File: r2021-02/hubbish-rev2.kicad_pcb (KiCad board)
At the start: 4 copper layers, 100 x 100 mm, 118 parts, among them J1 Conn_01x06, J2 USB_A_Stacked, J3 USB_A_Stacked, J4 USB_A (female down), J5 Conn_01x03_Male, J6 USB_A_Stacked, J8 USB_A male UP, J9 USB_B_Micro (up), Q1 Si4435, U1 2k i2c eeprom, U10 NUP4202, U11 NUP4202, U12 NUP4202, U13 NUP4202, U14 NUP4202, U15 NUP4202, U16 NUP4202, U17 NUP4202, U18 SY8366H, U19 APL3511C, U2 SE5120ST33, U3 USB2517, U4 APL3511C, U5 APL3511C, U6 APL3511C, U7 APL3511C, U8 APL3511C, U9 APL3511C, Y1 24MHz

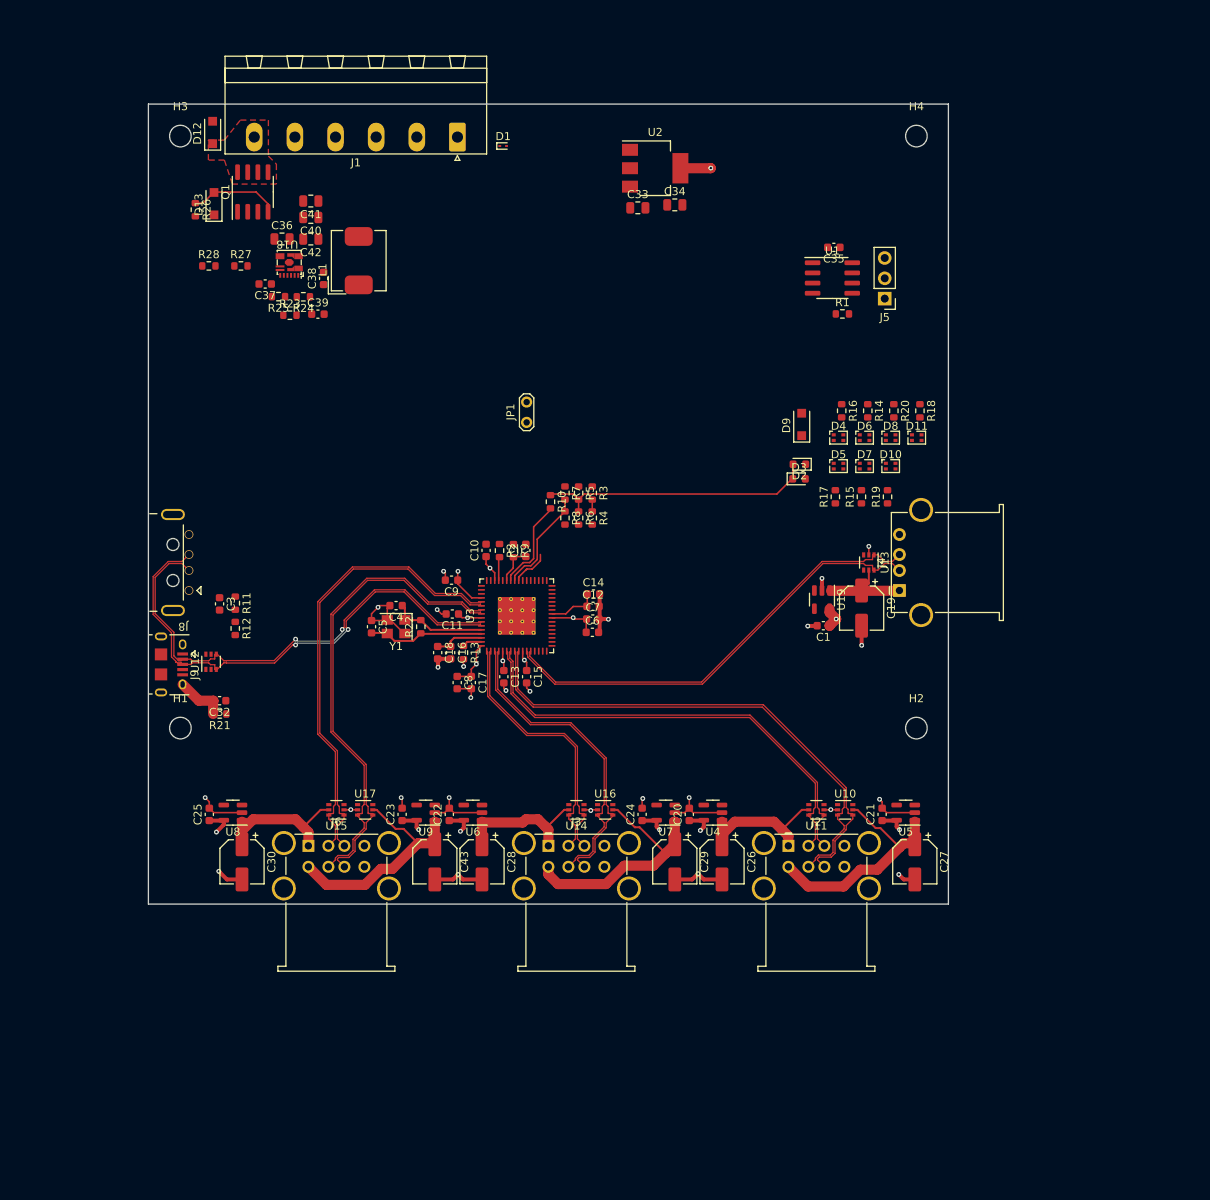
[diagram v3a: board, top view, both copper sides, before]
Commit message: r2021-02: "finish" routing
it's kinda untidy, but it's all routed out now, except for where I need
to replace the power supply
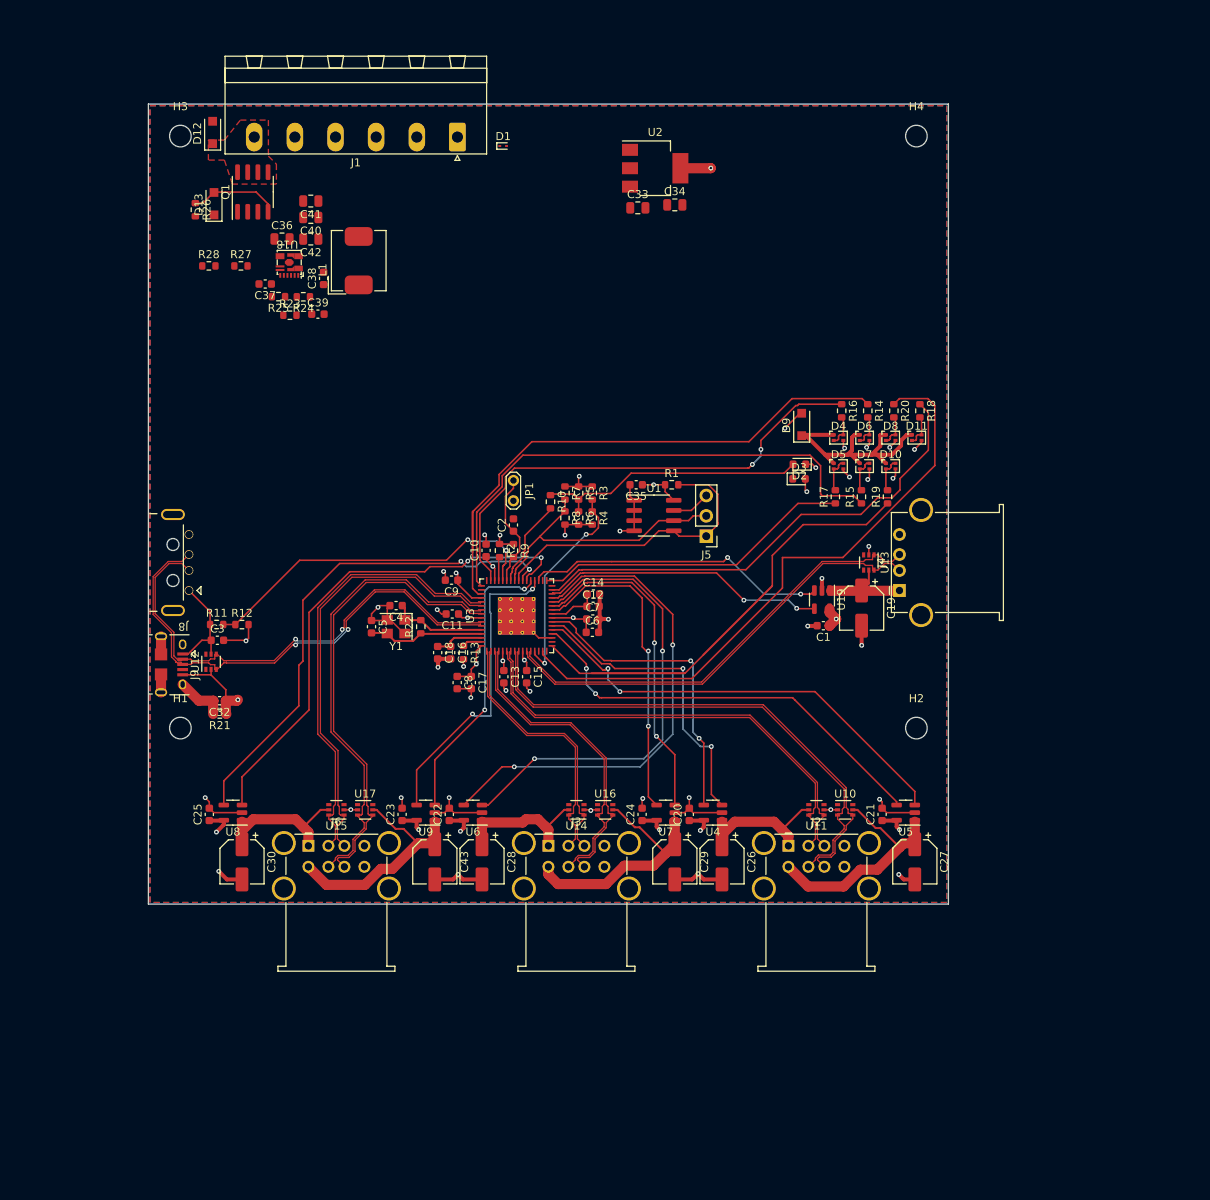
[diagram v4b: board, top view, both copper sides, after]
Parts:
- moved C35 38.6 mm to (141.0, 97.6)
- moved J5 37.1 mm to (149.7, 104.0)
- moved U1 37.1 mm to (143.2, 101.4)
- moved R1 30.2 mm to (145.4, 97.6)
- moved JP1 7.44 mm to (125.6, 97.0), turned to -90 degrees
- moved C3 4.55 mm to (88.6, 117.0), turned to 0 degrees
- moved R11 3.54 mm to (88.5, 115.1), turned to 0 degrees
- moved C2 3.53 mm to (125.6, 102.6)
- moved R12 0.97 mm to (91.7, 115.1), turned to 0 degrees
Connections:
- J5 pad 2: /upstream-config-leds/EE_SCL -> /upstream-config-leds/CFG_SEL0-EE_SCL
- U1 pad 6: /upstream-config-leds/EE_SCL -> /upstream-config-leds/CFG_SEL0-EE_SCL
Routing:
- net /upstream-config-leds/LED_A6: track 0.00 -> 78.3 mm
- net /upstream-config-leds/LED_A7: track 0.00 -> 77.2 mm
- net /upstream-config-leds/LED_A1: track 0.00 -> 72.6 mm
- net /upstream-config-leds/LED_A2: track 0.00 -> 65.9 mm
- net /downstream-port-power/OC5: track 0.00 -> 63.2 mm, vias 0 -> 2
- net /downstream-port-power/EN3: track 0.00 -> 63.0 mm, vias 0 -> 2
- net /downstream-port-power/EN5: track 0.00 -> 62.7 mm, vias 0 -> 2
- net /upstream-config-leds/LED_A3: track 0.00 -> 61.8 mm, vias 0 -> 2
- net /upstream-config-leds/LED_A5: track 0.00 -> 61.3 mm
- net /downstream-port-power/OC3: track 0.00 -> 58.9 mm, vias 0 -> 2
- net /downstream-port-power/OC2: track 0.00 -> 56.4 mm, vias 0 -> 2
- net /downstream-port-power/EN2: track 0.00 -> 53.7 mm, vias 0 -> 2
- net GND: track 86.7 -> 134.5 mm, vias 26 -> 39
- net /upstream-config-leds/VBUS_DET: track 0.00 -> 44.2 mm, vias 0 -> 2
- net /downstream-port-power/OC4: track 0.00 -> 41.2 mm, vias 0 -> 2
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- added copper zone on In2.Cu, net +3V3
- added copper zone on B.Cu, net GND
- added copper zone on F.Cu, net GND

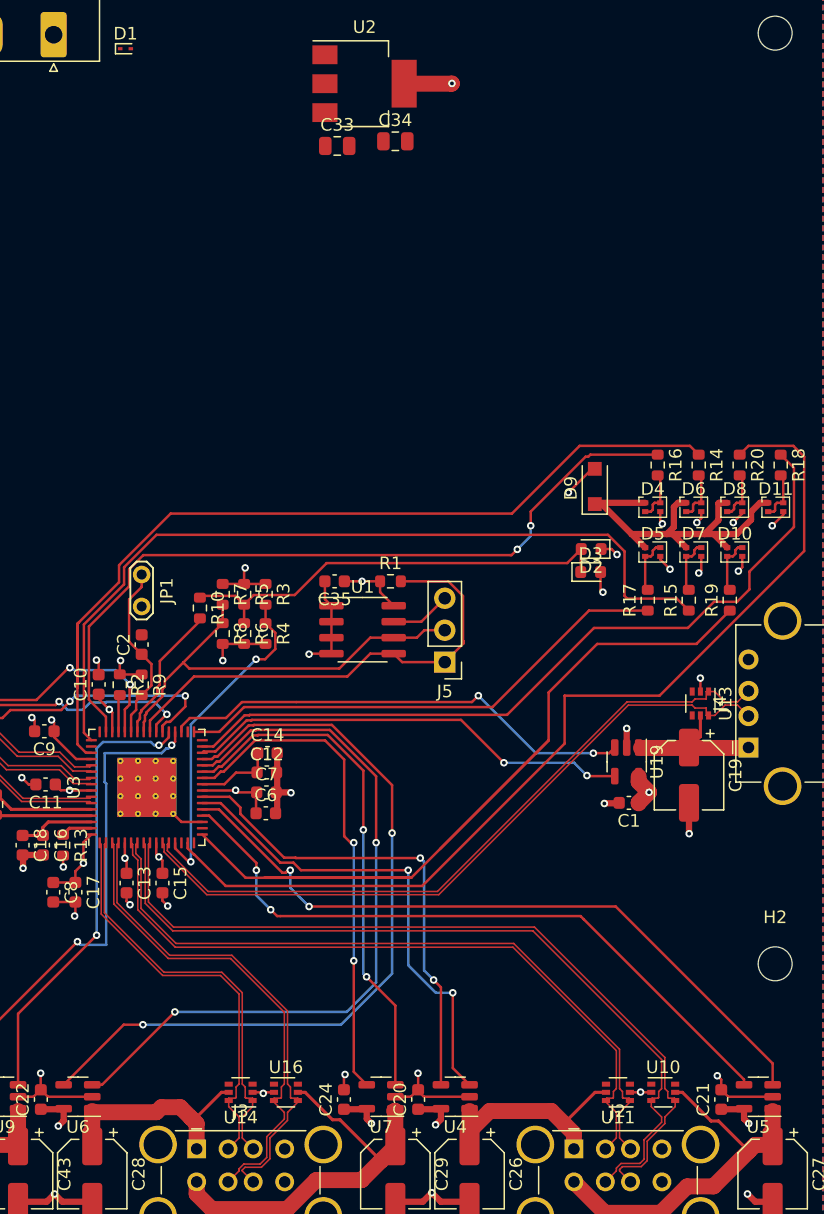
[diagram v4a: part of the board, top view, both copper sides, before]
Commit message: hw-rev2: break out power input to a new sheet
It was always a bit crowded there, and now that we need to pick new
parts, we want a little more space...
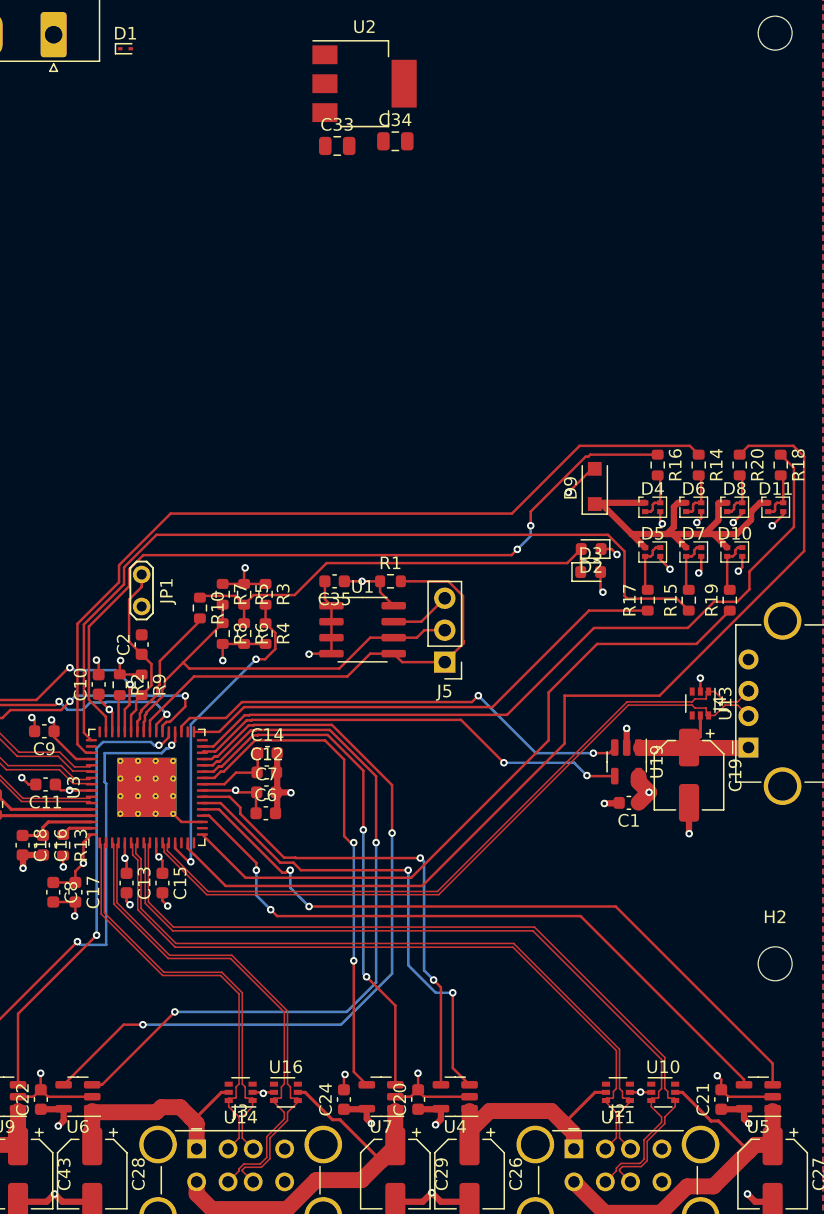
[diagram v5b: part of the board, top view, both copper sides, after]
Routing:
- net /upstream-config-leds/LED_A6: track 78.3 -> 54.4 mm
- net /upstream-config-leds/LED_A1: track 72.6 -> 67.3 mm
- net +3V3: track 50.4 -> 46.3 mm, vias 13 -> 12

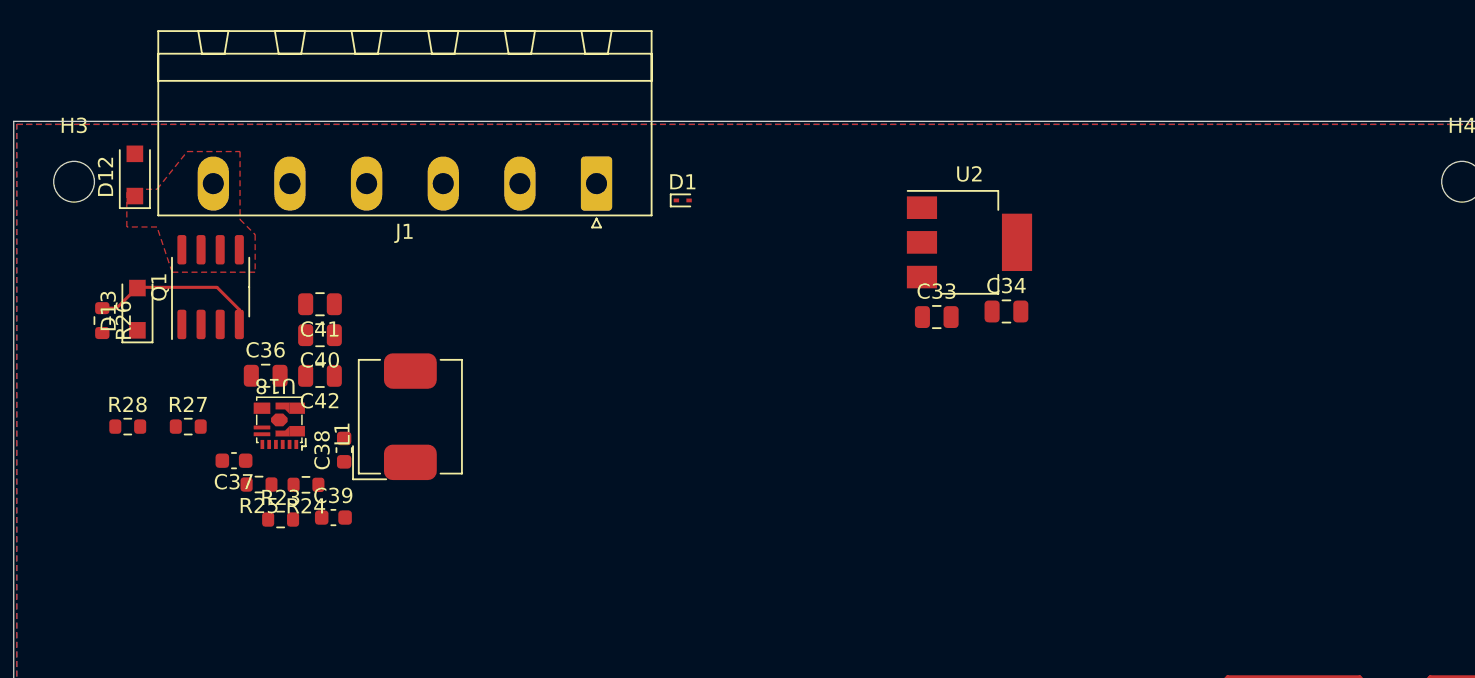
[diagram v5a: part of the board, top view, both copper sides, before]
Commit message: hw: r2: use SiC437 for power supply
Overhaul heavily.  Schematic largely complete for changes, but needs
review, PCB barely started.
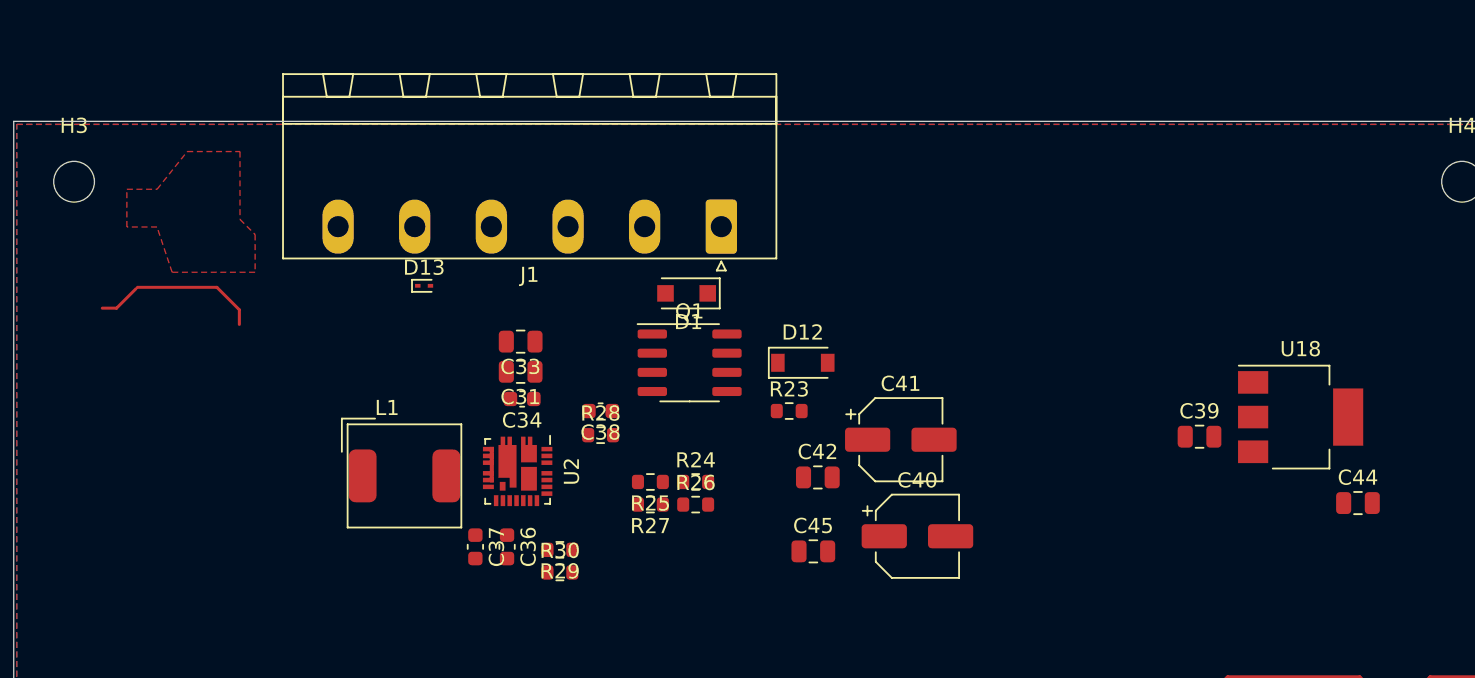
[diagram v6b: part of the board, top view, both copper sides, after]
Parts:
- added C31: 22uF/30V+, Capacitor_SMD:C_0805_2012Metric, F.Cu at (113.6, 66.6)
- added C44: 10uF, Capacitor_SMD:C_0805_2012Metric, F.Cu at (169.1, 75.3)
- added C45: 22uF/6.3V, Capacitor_SMD:C_0805_2012Metric, F.Cu at (133.0, 78.5)
- added R29: 22k, Resistor_SMD:R_0603_1608Metric, F.Cu at (116.2, 78.4)
- added R30: 3k, Resistor_SMD:R_0603_1608Metric, F.Cu at (116.2, 79.9)
- C33: value 10uF -> 22uF/30V+
- C34: value 10uF -> .1uF; footprint Capacitor_SMD:C_0805_2012Metric -> Capacitor_SMD:C_0603_1608Metric
- C36: value 10uF/50V -> 1uF; footprint Capacitor_SMD:C_0805_2012Metric -> Capacitor_SMD:C_0603_1608Metric
- C37: value 2.2uF -> 4.7uF
- C38: value 100nF -> .1uF
- C39: value Cff -> 10uF; footprint Capacitor_SMD:C_0603_1608Metric -> Capacitor_SMD:C_0805_2012Metric
- C40, C41: value 22uF/6.3V -> 100uF; footprint Capacitor_SMD:C_0805_2012Metric -> Capacitor_SMD:CP_Elec_5x5.4
- D1: value DF2S6.2FS,L3M -> SMF24A; footprint Diode_SMD:D_SOD-923 -> Diode_SMD:D_SOD-123F
- D12: value SMF24A -> BZT52B12; footprint Diode_SMD:D_SOD-123F -> Diode_SMD:D_SOD-123
- D13: value 6.8V Zener or so -> DF2S6.2FS,L3M; footprint Diode_SMD:D_SOD-123F -> Diode_SMD:D_SOD-923
- L1: value 2.2uH -> 1.5uH; footprint Inductor_SMD:L_CHILISIN_BMRx00060630 -> Inductor_SMD:L_AVX_LMLP07A7
- R23: value Rff -> 10k
- R24: value 100k/1% -> DNP
- R25: value 13k6/1% -> 100k
- R26: value 330 -> DNP
- R27: value 100k -> 499k
- R28: value 100k -> 2.2
- U18: value SY8366H -> SE5120ST33; footprint et-parts:SY8366H -> Package_TO_SOT_SMD:SOT-223-3_TabPin2
- U2: value SE5120ST33 -> SiC437AED; footprint Package_TO_SOT_SMD:SOT-223-3_TabPin2 -> Package_DFN_QFN:Vishay_MLP-44L_4x4
- moved U18 67.7 mm to (165.3, 69.6), turned to 0 degrees
- moved C39 57.7 mm to (158.6, 70.9)
- moved D12 46.0 mm to (132.3, 66.0), turned to 0 degrees
- moved C40 41.8 mm to (139.9, 77.5), turned to 0 degrees
- moved R26 41.2 mm to (125.2, 75.4), turned to 0 degrees
- moved C41 39.5 mm to (138.8, 71.1), turned to 0 degrees
- moved R23 34.5 mm to (131.4, 69.2)
- moved C42 33.7 mm to (133.3, 73.6), turned to 0 degrees
- moved U2 33.6 mm to (113.4, 73.2), turned to -90 degrees
- moved C34 32.6 mm to (113.7, 68.4), turned to 180 degrees
- moved Q1 32.1 mm to (124.8, 66.0), turned to 0 degrees
- moved R28 31.3 mm to (118.9, 70.8)
- moved R27 31.1 mm to (122.2, 75.4), turned to 180 degrees
- moved C33 27.6 mm to (113.6, 64.6), turned to 180 degrees
- moved R25 25.9 mm to (122.2, 73.9)
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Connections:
- C33 pad 1: +5V -> +VDC
- C34 pad 1: +3V3 -> +VDC
- C34 pad 2: GND -> GNDA
- C36 pad 1: +VDC -> /power_input/VDD
- C36 pad 2: GND -> GNDA
- C37 pad 1: /upstream-config-leds/SY-VCC -> /power_input/VDRV
- C38 pad 1: /upstream-config-leds/BST -> Net-(C38-Pad1)
- C38 pad 2: /upstream-config-leds/LX -> /power_input/phase
- C39 pad 1: Net-(C39-Pad1) -> +5V
- C39 pad 2: +5V -> GND
- D1 pad 1: +5V -> /power_input/PWR_RAW
- D12 pad 1: /upstream-config-leds/PWR_RAW -> +VDC
- D12 pad 2: GND -> /power_input/PolProtG
- D13 pad 1: +VDC -> +5V
- D13 pad 2: /upstream-config-leds/PolProtG -> GND
- J1 pad 1: +5V -> /power_input/PWR_RAW
- J1 pad 2: +5V -> /power_input/PWR_RAW
- J1 pad 5: GND -> +5V
- J1 pad 6: /upstream-config-leds/PWR_RAW -> +5V
- L1 pad 1: /upstream-config-leds/LX -> +5V
- L1 pad 2: +5V -> /power_input/SW
- Q1 pad 4: /upstream-config-leds/PolProtG -> /power_input/PolProtG
- Q1 pad 5: /upstream-config-leds/PWR_RAW -> /power_input/PWR_RAW
- Q1 pad 6: /upstream-config-leds/PWR_RAW -> /power_input/PWR_RAW
- Q1 pad 7: /upstream-config-leds/PWR_RAW -> /power_input/PWR_RAW
- Q1 pad 8: /upstream-config-leds/PWR_RAW -> /power_input/PWR_RAW
- R23 pad 1: /upstream-config-leds/SY-FB -> /power_input/PolProtG
- R23 pad 2: Net-(C39-Pad1) -> GND
- R24 pad 1: +5V -> /power_input/MODE2
- R24 pad 2: /upstream-config-leds/SY-FB -> /power_input/VDD
- R25 pad 1: /upstream-config-leds/SY-FB -> GNDA
- R25 pad 2: GND -> /power_input/MODE2
- R26 pad 1: /upstream-config-leds/PolProtG -> /power_input/MODE1
- R26 pad 2: GND -> /power_input/VDD
- R27 pad 1: GND -> GNDA
- R27 pad 2: Net-(R27-Pad2) -> /power_input/MODE1
- R28 pad 1: /upstream-config-leds/SY-VCC -> /power_input/boot
- R28 pad 2: Net-(R27-Pad2) -> Net-(C38-Pad1)
- U18 pad 2: /upstream-config-leds/LX -> +3V3
- U18 pad 3: unconnected-(U18-Pad3) -> +5V
- U2 pad 1: GND -> +VDC
- U2 pad 3: +5V -> GND
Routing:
- net /upstream-config-leds/PolProtG: track 11.1 -> 0.00 mm
- net (no net): track 0.00 -> 11.1 mm
- added copper zone on F.Cu, net (none)
- removed copper zone on F.Cu, net /upstream-config-leds/PWR_RAW
